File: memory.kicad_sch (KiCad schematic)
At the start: 11 parts

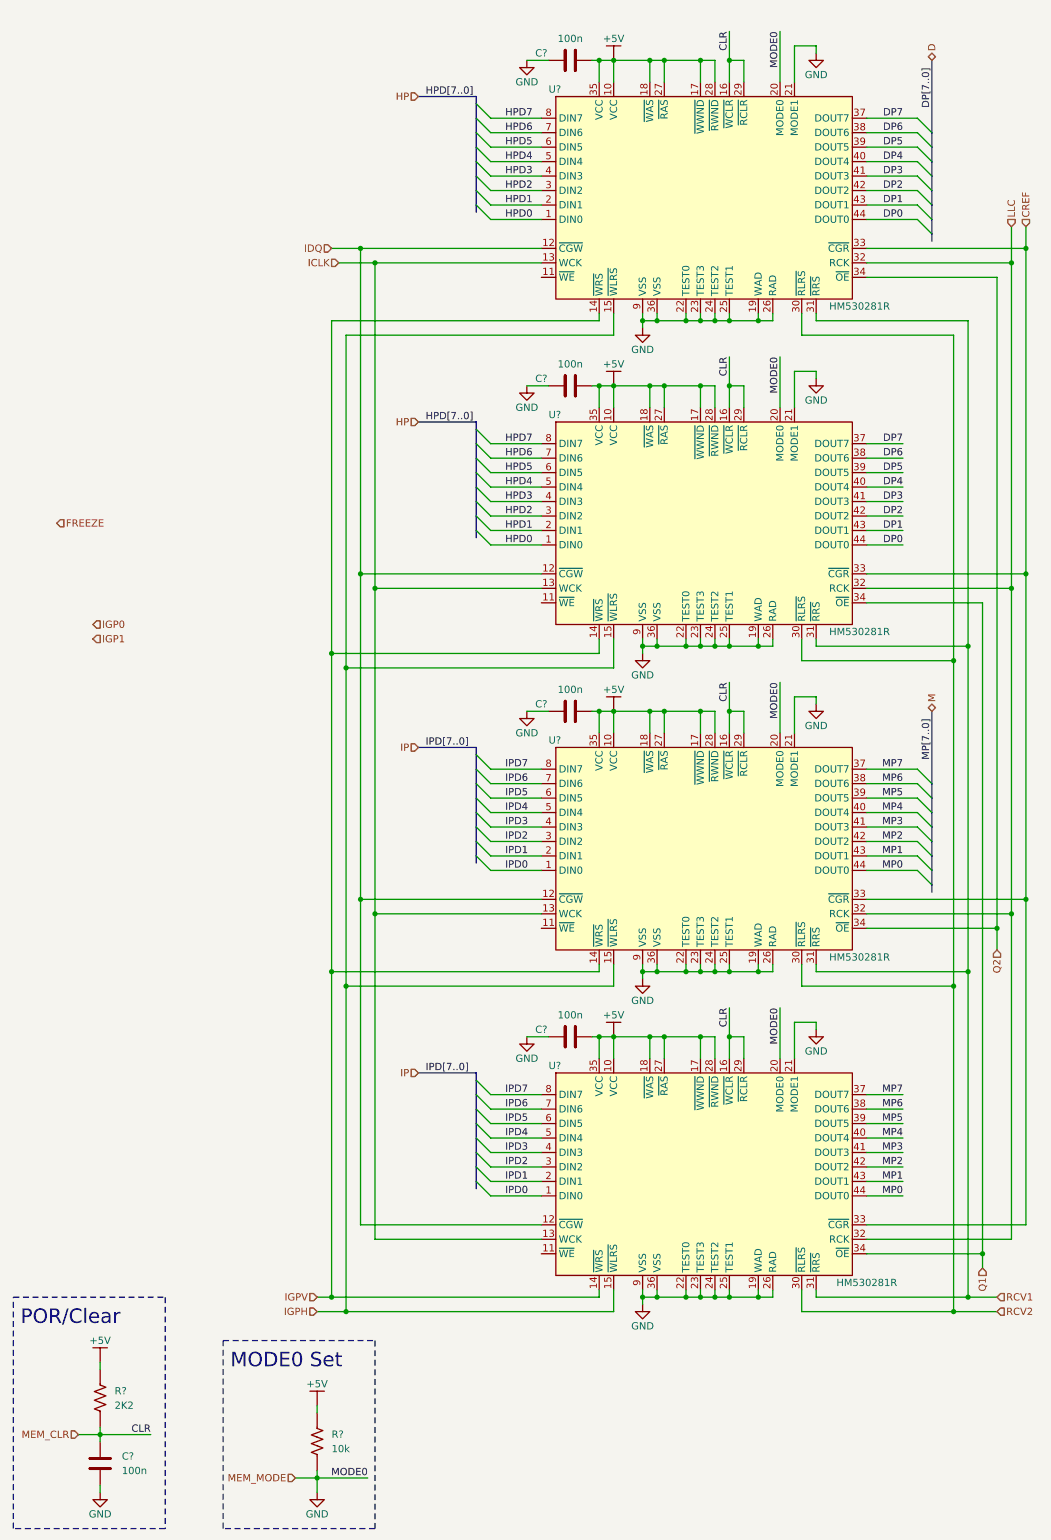
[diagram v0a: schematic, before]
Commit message: minor changes to schematic layout
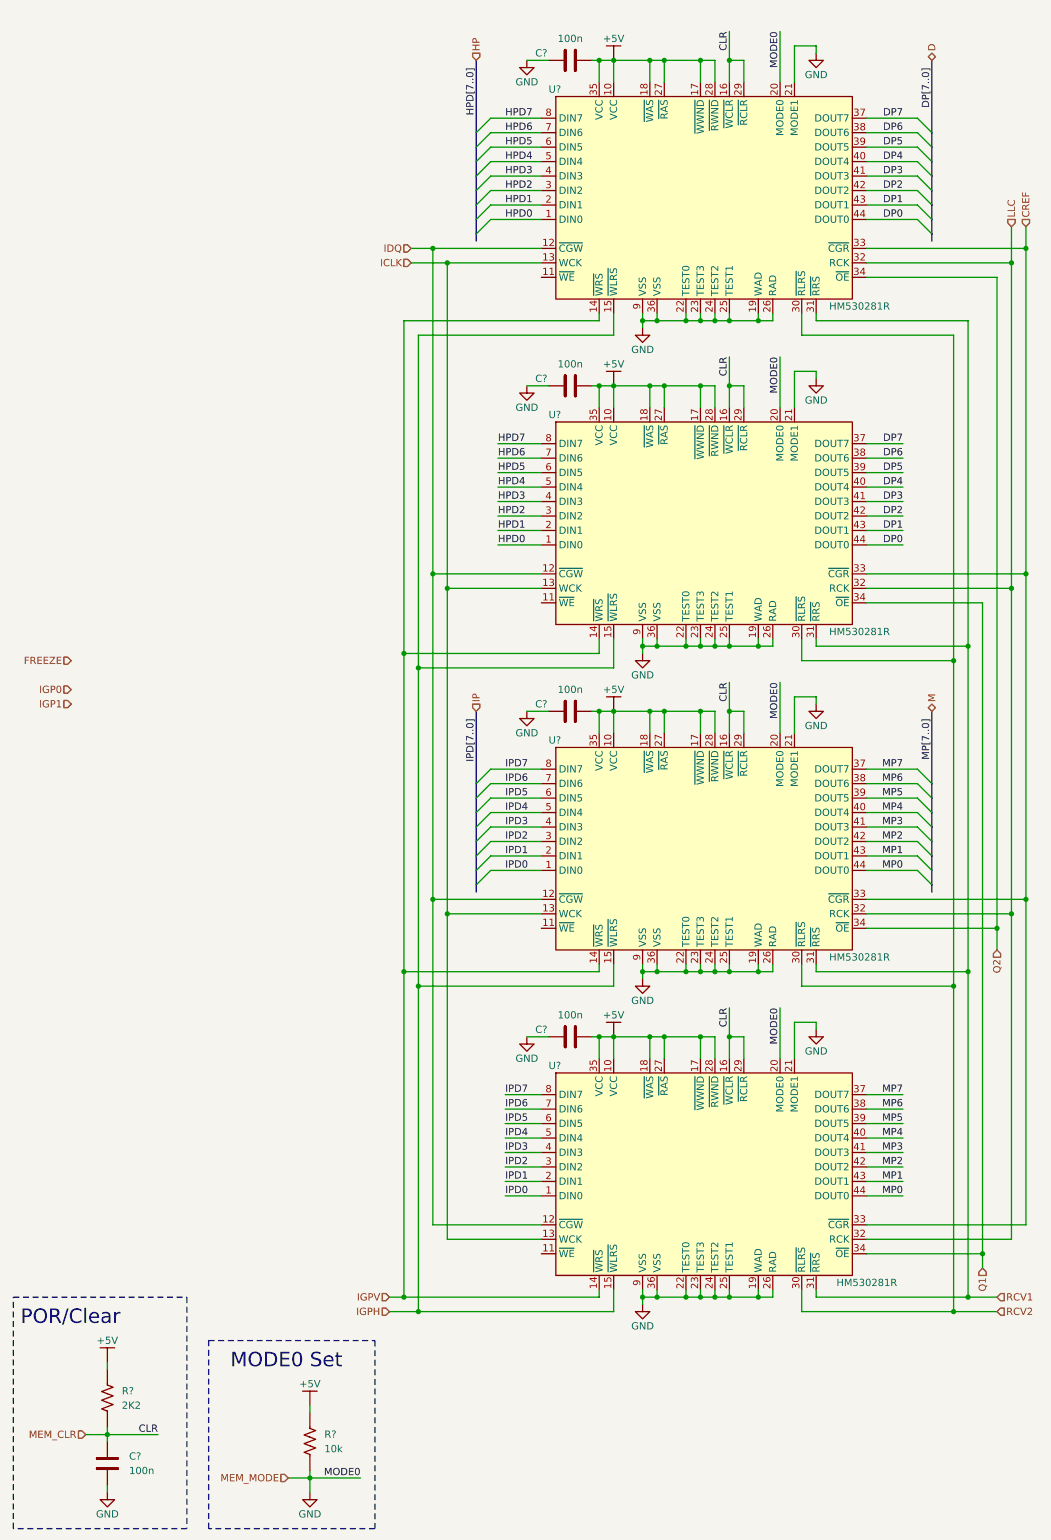
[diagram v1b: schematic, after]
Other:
- moved on the sheet: C?, R?

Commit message: added connectors and crystal, osc
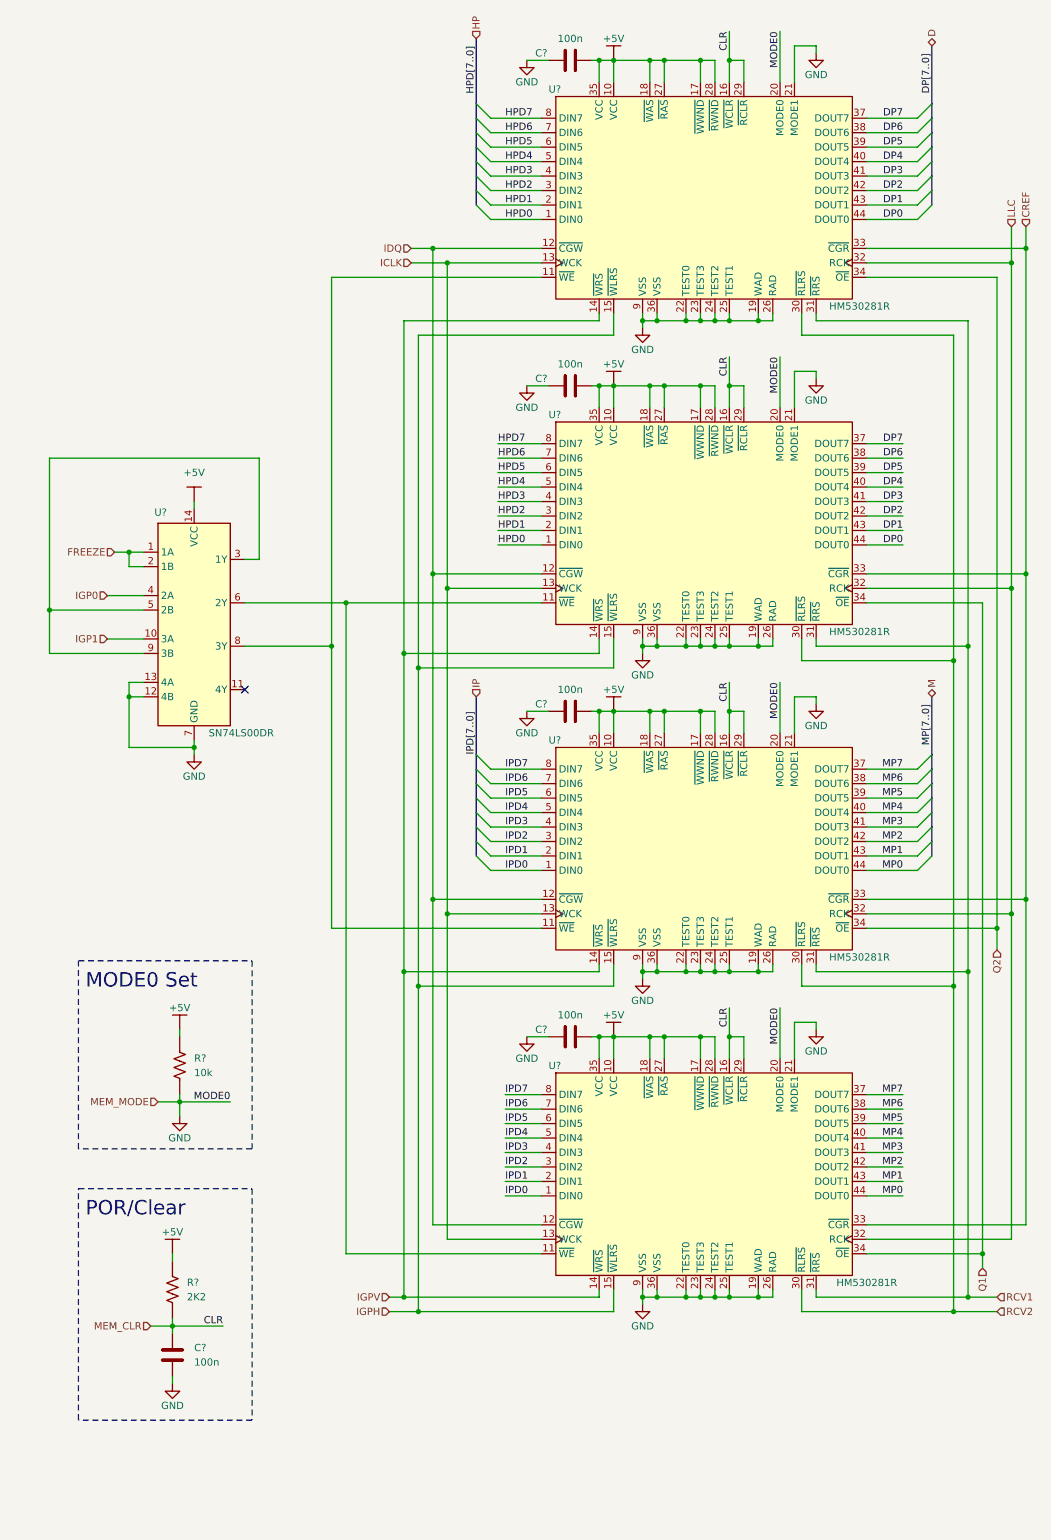
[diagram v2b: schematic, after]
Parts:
- added U?: SN74LS00DR, symbol tbc:SN74LS00DR
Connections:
- net +5V: now also U?.14 (VCC)
- net FREEZE: now also U?.1 (1A), U?.2 (1B)
- net GND: now also U?.12 (4B), U?.13 (4A), U?.7 (GND)
- net IGP0: now also U?.4 (2A)
- net IGP1: now also U?.10 (3A)
- net at U?.11 (~{WE}): now also U?.11 (~{WE}), U?.8 (3Y)
- net at U?.11 (~{WE}): now also U?.11 (~{WE}), U?.6 (2Y)
- new net: U?.3 (1Y), U?.5 (2B), U?.9 (3B)
- no-connect marks 0 -> 1
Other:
- moved on the sheet: C?, R?

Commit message: completed and annotated schematic, passed ERC
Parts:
- gave numbers to parts that had none: 12
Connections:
- net GND: no longer R12.1, U3.20 (MODE0), U4.20 (MODE0), U5.20 (MODE0), U6.20 (MODE0)
- new net MEM_MODE: R12.1, U3.20 (MODE0), U4.20 (MODE0), U5.20 (MODE0), U6.20 (MODE0)
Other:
- moved on the sheet: C22, R11, R12

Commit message: minor cleanup, addition of notes
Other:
- moved on the sheet: C22, R11, R12

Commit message: added footprints for large ICs
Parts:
- U3, U4, U5, U6: footprint (none) -> tbc:TTP-44DB
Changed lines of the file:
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@@
       (effects (font (size 1.27 1.27)))
     )
-    (property "Footprint" "" (at 137.16 162.56 0)
+    (property "Footprint" "tbc:TTP-44DB" (at 137.16 162.56 0)
       (effects (font (size 1.27 1.27)) hide)
     )
@@
       (effects (font (size 1.27 1.27)))
     )
-    (property "Footprint" "" (at 137.16 105.41 0)
+    (property "Footprint" "tbc:TTP-44DB" (at 137.16 105.41 0)
       (effects (font (size 1.27 1.27)) hide)
     )
@@
       (effects (font (size 1.27 1.27)))
     )
-    (property "Footprint" "" (at 137.16 219.71 0)
+    (property "Footprint" "tbc:TTP-44DB" (at 137.16 219.71 0)
       (effects (font (size 1.27 1.27)) hide)
     )
@@
       (effects (font (size 1.27 1.27)))
     )
-    (property "Footprint" "" (at 137.16 48.26 0)
-      (effects (font (size 1.27 1.27)) hide)
-    )
+    (property "Footprint" "tbc:TTP-44DB" (at 137.16 48.26 0)
+      (effects (font (size 1.27 1.27)) hide)
+    )

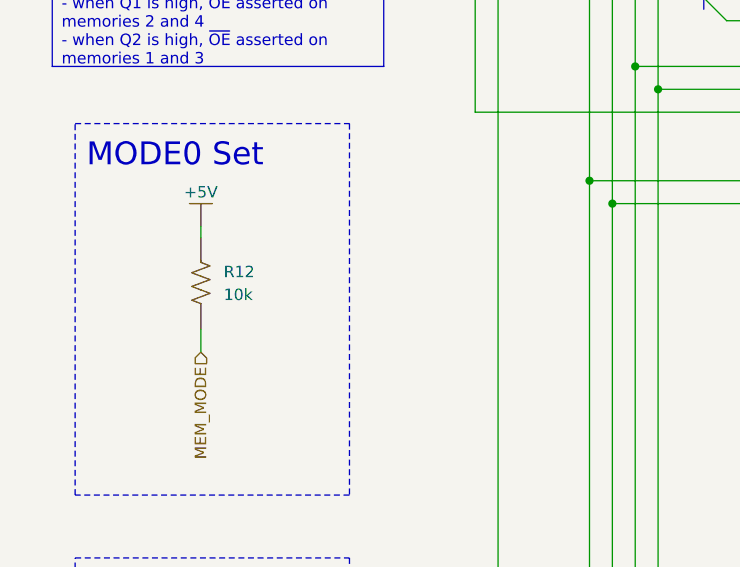
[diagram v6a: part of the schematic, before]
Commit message: resistor footprint added
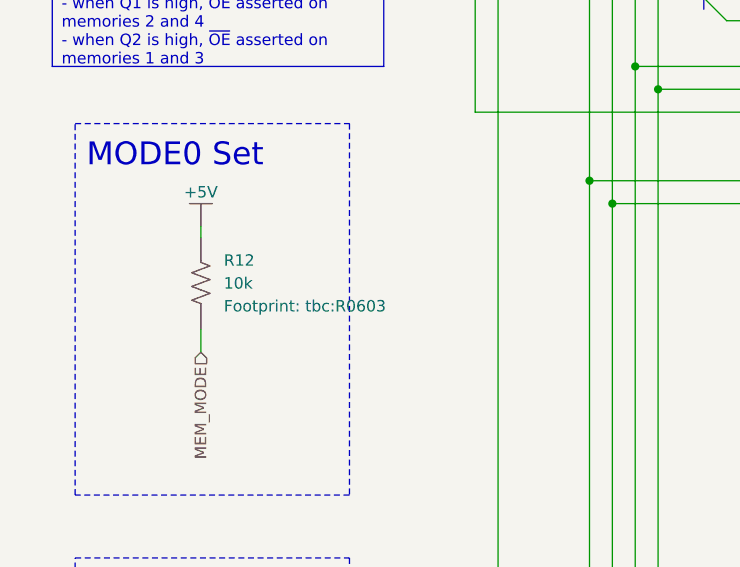
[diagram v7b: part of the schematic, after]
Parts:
- R11, R12: footprint (none) -> tbc:R0603
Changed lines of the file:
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@@
       (effects (font (size 1.27 1.27)) (justify right))
     )
-    (property "Footprint" "" (at 52.07 260.35 0)
+    (property "Footprint" "tbc:R0603" (at 52.07 243.84 0) (show_name)
       (effects (font (size 1.27 1.27)) hide)
     )
@@
   (symbol (lib_id "tbc:RC0603FR-0710KL") (at 40.64 195.58 90) (unit 1)
     (in_bom yes) (on_board yes) (dnp no) (fields_autoplaced)
-    (property "Reference" "R12" (at 43.18 194.2782 90)
-      (effects (font (size 1.27 1.27)) (justify right))
-    )
-    (property "Value" "10k" (at 43.18 196.8182 90)
-      (effects (font (size 1.27 1.27)) (justify right))
-    )
-    (property "Footprint" "" (at 48.26 212.09 0)
-      (effects (font (size 1.27 1.27)) hide)
+    (property "Reference" "R12" (at 43.18 193.0082 90)
+      (effects (font (size 1.27 1.27)) (justify right))
+    )
+    (property "Value" "10k" (at 43.18 195.5482 90)
+      (effects (font (size 1.27 1.27)) (justify right))
+    )
+    (property "Footprint" "tbc:R0603" (at 43.18 198.0882 90) (show_name)
+      (effects (font (size 1.27 1.27)) (justify right))
     )
     (property "Datasheet" "https://www.mouser.com/datasheet/2/447/YAGEO_PYu_RC_Group_51_RoHS_L_12-3313492.pdf" (at 53.34 212.09 0) (show_name)

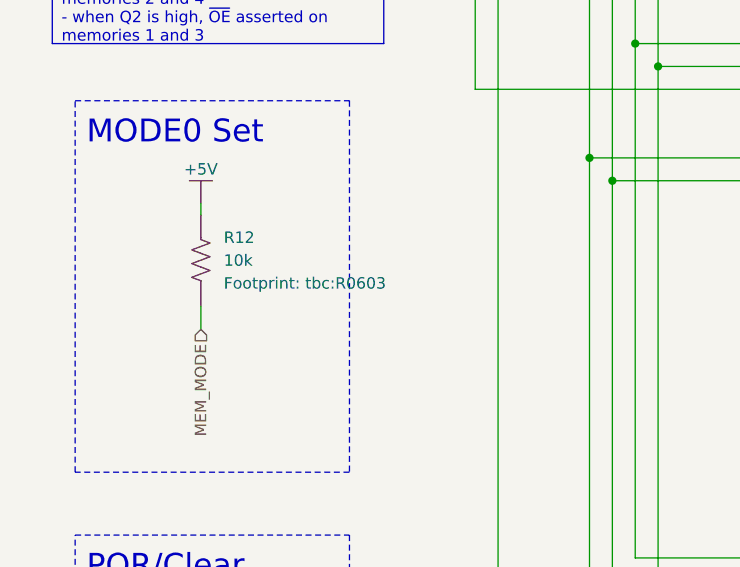
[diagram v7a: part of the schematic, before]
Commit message: footprints and 3d models for caps, connectors
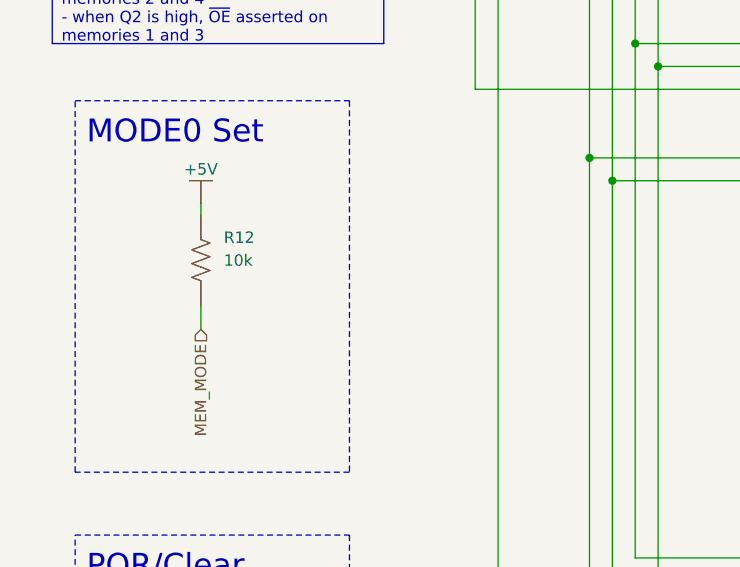
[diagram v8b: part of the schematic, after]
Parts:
- C22, C23, C24, C25, C26: footprint (none) -> tbc:C0603
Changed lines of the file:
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@@
       (effects (font (size 1.27 1.27)))
     )
-    (property "Footprint" "" (at 113.03 35.56 0)
+    (property "Footprint" "tbc:C0603" (at 113.03 35.56 0)
       (effects (font (size 1.27 1.27)) hide)
     )
@@
       (effects (font (size 1.27 1.27)))
     )
-    (property "Footprint" "" (at 113.03 149.86 0)
+    (property "Footprint" "tbc:C0603" (at 113.03 149.86 0)
       (effects (font (size 1.27 1.27)) hide)
     )
@@
       (effects (font (size 1.27 1.27)))
     )
-    (property "Footprint" "" (at 113.03 207.01 0)
+    (property "Footprint" "tbc:C0603" (at 113.03 207.01 0)
       (effects (font (size 1.27 1.27)) hide)
     )
@@
       (effects (font (size 1.27 1.27)))
     )
-    (property "Footprint" "" (at 113.03 92.71 0)
+    (property "Footprint" "tbc:C0603" (at 113.03 92.71 0)
       (effects (font (size 1.27 1.27)) hide)
     )
@@
       (effects (font (size 1.27 1.27)) (justify right))
     )
-    (property "Footprint" "" (at 55.88 255.27 0)
+    (property "Footprint" "tbc:C0603" (at 55.88 255.27 0)
       (effects (font (size 1.27 1.27)) hide)
     )
@@
     )
     (property "Footprint" "tbc:R0603" (at 43.18 198.0882 90) (show_name)
-      (effects (font (size 1.27 1.27)) (justify right))
+      (effects (font (size 1.27 1.27)) (justify right) hide)
     )
     (property "Datasheet" "https://www.mouser.com/datasheet/2/447/YAGEO_PYu_RC_Group_51_RoHS_L_12-3313492.pdf" (at 53.34 212.09 0) (show_name)
